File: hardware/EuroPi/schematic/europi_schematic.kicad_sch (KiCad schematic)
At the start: 110 parts, among them J1 Output 1 Jack, J2 Output 2 Jack, J3 Output 3 Jack, J4 Output 4 Jack, J5 Output 5 Jack, J6 Output 6 Jack, J7 Digital Input Jack, J8 Analogue Input Jack, Q1 2N2222, SW1 SW_Push, SW2 SW_Push

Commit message: create kicad project
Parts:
- removed D1, D2, D3, D4: ${SIM.PARAMS}, symbol Simulation_SPICE:DIODE
- removed Reference? (x5): +12V, symbol text:TEXT
- removed Reference? (x2): +5V, symbol text:TEXT
- removed Reference? (x9): +3.3V, symbol text:TEXT
- added C15: 1nF, Capacitor_SMD:C_0603_1608Metric, symbol Device:C
- added D1, D2, D3, D5: D, symbol Device:D
- added J2: Conn_01x04_Pin, symbol Connector:Conn_01x04_Pin
- C1: renamed from C15; footprint (none) -> Capacitor_SMD:C_0603_1608Metric
- C10: renamed from C7; footprint (none) -> Capacitor_SMD:C_0603_1608Metric
- C11: renamed from C9; footprint (none) -> Capacitor_SMD:C_0603_1608Metric
- C12: footprint (none) -> Capacitor_SMD:C_0603_1608Metric
- C13: renamed from C10; footprint (none) -> Capacitor_SMD:C_0603_1608Metric
- C14: renamed from C13; footprint (none) -> Capacitor_SMD:C_0603_1608Metric
- C16: renamed from C11; footprint (none) -> Capacitor_SMD:C_0603_1608Metric
- C17: renamed from C14; footprint (none) -> Capacitor_SMD:C_0603_1608Metric
- C2: renamed from C16; footprint (none) -> Capacitor_SMD:C_0603_1608Metric
- C3: renamed from C2; footprint (none) -> Capacitor_SMD:C_0603_1608Metric
- C4: renamed from C3; footprint (none) -> Capacitor_SMD:C_0603_1608Metric
- C5: renamed from C4; footprint (none) -> Capacitor_SMD:C_0603_1608Metric
- C6: renamed from C5; footprint (none) -> Capacitor_SMD:C_0603_1608Metric
- C7: renamed from C6; footprint (none) -> Capacitor_SMD:C_0603_1608Metric
- C8: renamed from C1; footprint (none) -> Capacitor_SMD:C_0603_1608Metric
- C9: renamed from C8; footprint (none) -> Capacitor_SMD:C_0603_1608Metric
- J1: renamed from J?; footprint (none) -> Connector_PinHeader_2.54mm:PinHeader_2x08_P2.54mm_Vertical
- J10: renamed from J6; footprint (none) -> Connector_Audio:Jack_3.5mm_QingPu_WQP-PJ398SM_Vertical_CircularHoles
- J3: renamed from J1; footprint (none) -> Connector_Audio:Jack_3.5mm_QingPu_WQP-PJ398SM_Vertical_CircularHoles
- J4: footprint (none) -> Connector_Audio:Jack_3.5mm_QingPu_WQP-PJ398SM_Vertical_CircularHoles
- J5: renamed from J8; footprint (none) -> Connector_Audio:Jack_3.5mm_QingPu_WQP-PJ398SM_Vertical_CircularHoles
- J6: renamed from J2; footprint (none) -> Connector_Audio:Jack_3.5mm_QingPu_WQP-PJ398SM_Vertical_CircularHoles
- J7: renamed from J5; footprint (none) -> Connector_Audio:Jack_3.5mm_QingPu_WQP-PJ398SM_Vertical_CircularHoles
- J8: renamed from J7; footprint (none) -> Connector_Audio:Jack_3.5mm_QingPu_WQP-PJ398SM_Vertical_CircularHoles
- J9: renamed from J3; footprint (none) -> Connector_Audio:Jack_3.5mm_QingPu_WQP-PJ398SM_Vertical_CircularHoles
- LED1, LED6: footprint (none) -> LED_THT:LED_D3.0mm
- LED2: renamed from LED4; footprint (none) -> LED_THT:LED_D3.0mm
- LED3: renamed from LED2; footprint (none) -> LED_THT:LED_D3.0mm
- LED4: renamed from LED5; footprint (none) -> LED_THT:LED_D3.0mm
- LED5: renamed from LED3; footprint (none) -> LED_THT:LED_D3.0mm
- R1: renamed from R20; footprint (none) -> Resistor_SMD:R_0603_1608Metric
- R10: renamed from R38; footprint (none) -> Resistor_SMD:R_0603_1608Metric
- R11: renamed from R13; footprint (none) -> Resistor_SMD:R_0603_1608Metric
- R12: renamed from R16; footprint (none) -> Resistor_SMD:R_0603_1608Metric
- R13: renamed from R7; footprint (none) -> Resistor_SMD:R_0603_1608Metric
- R14: renamed from R10; footprint (none) -> Resistor_SMD:R_0603_1608Metric
- R15: renamed from R28; footprint (none) -> Resistor_SMD:R_0603_1608Metric
- R16: renamed from R2; footprint (none) -> Resistor_SMD:R_0603_1608Metric
- R17: renamed from R5; footprint (none) -> Resistor_SMD:R_0603_1608Metric
- R18: renamed from R21; footprint (none) -> Resistor_SMD:R_0603_1608Metric
- R19: renamed from R30; footprint (none) -> Resistor_SMD:R_0603_1608Metric
- R2: renamed from R19; footprint (none) -> Resistor_SMD:R_0603_1608Metric
- R20: renamed from R33; footprint (none) -> Resistor_SMD:R_0603_1608Metric
- R21: renamed from R36; footprint (none) -> Resistor_SMD:R_0603_1608Metric
- R22: renamed from R39; footprint (none) -> Resistor_SMD:R_0603_1608Metric
- R23: renamed from R22; footprint (none) -> Resistor_SMD:R_0603_1608Metric
- R24: renamed from R14; footprint (none) -> Resistor_SMD:R_0603_1608Metric
- R25: renamed from R17; footprint (none) -> Resistor_SMD:R_0603_1608Metric
- R26: renamed from R8; footprint (none) -> Resistor_SMD:R_0603_1608Metric
- R27: renamed from R11; footprint (none) -> Resistor_SMD:R_0603_1608Metric
- R28: renamed from R23; footprint (none) -> Resistor_SMD:R_0603_1608Metric
- R29: renamed from R3; footprint (none) -> Resistor_SMD:R_0603_1608Metric
- R3: renamed from R1; footprint (none) -> Resistor_SMD:R_0603_1608Metric
- R30: renamed from R6; footprint (none) -> Resistor_SMD:R_0603_1608Metric
- R31, R4: footprint (none) -> Resistor_SMD:R_0603_1608Metric
- R32: renamed from R34; footprint (none) -> Resistor_SMD:R_0603_1608Metric
- R33: renamed from R37; footprint (none) -> Resistor_SMD:R_0603_1608Metric
- R34: renamed from R40; footprint (none) -> Resistor_SMD:R_0603_1608Metric
- R35: renamed from R27; footprint (none) -> Resistor_SMD:R_0603_1608Metric
- R36: renamed from R15; footprint (none) -> Resistor_SMD:R_0603_1608Metric
- R37: renamed from R18; footprint (none) -> Resistor_SMD:R_0603_1608Metric
- R38: renamed from R9; footprint (none) -> Resistor_SMD:R_0603_1608Metric
- R39: renamed from R12; footprint (none) -> Resistor_SMD:R_0603_1608Metric
- R40: renamed from R26; footprint (none) -> Resistor_SMD:R_0603_1608Metric
- R5: renamed from R24; footprint (none) -> Resistor_SMD:R_0603_1608Metric
- R6: renamed from R25; footprint (none) -> Resistor_SMD:R_0603_1608Metric
- R7: renamed from R29; footprint (none) -> Resistor_SMD:R_0603_1608Metric
- R8: renamed from R32; footprint (none) -> Resistor_SMD:R_0603_1608Metric
- R9: renamed from R35; footprint (none) -> Resistor_SMD:R_0603_1608Metric
- U2: renamed from U?; footprint (none) -> Module:RaspberryPi_Pico_Common_THT
- VR1, VR2: footprint (none) -> Potentiometer_THT:Potentiometer_Alpha_RD901F-40-00D_Single_Vertical
- gave numbers to parts that had none: 6
- renumbered O1 to O4, O to O5
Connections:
- net GP16 is gone; now on net OUT_3: R29.2
- net GP17 is gone; now on net OUT_4: R4.2
- net GP18 is gone; now on net OUT_5: R17.2
- net GP19 is gone; now on net OUT_6: R30.2
- net GP20 is gone; now on net OUT_2: R16.2
- net GP21 is gone; now on net OUT_1: R3.2
- net GP22 is gone; now on net DIGITAL_IN: Q1.3 (C), R40.2
- net GP26 is gone; now on net ANALOGUE_IN: O4.1, R28.2
- net GP27 is gone; now on net KNOB_1: VR1.2
- net GP28 is gone; now on net KNOB_2: VR2.2
- net GP4 is gone; now on net BUTTON_1: C9.1, R1.1, R5.1
- net GP5 is gone; now on net BUTTON_2: C10.1, R2.1, R6.1
- net -12V: now also D1.2 (A)
- net GND: now also J5.S, D3.2 (A)
- net +12V: now reaches C1.1, C4.1, C6.1
- net +12V: now also O1.4 (V+), O3.4 (V+), U1.1 (IN), D5.1 (K)
- net OLED_SDA: now reaches U2.1 (GP0)
- net DIN_DETECT: now reaches U2.10 (GP7)
- net DIN_DETECT: now also J8.TN
- net OLED_SCL: now reaches U2.2 (GP1)
- net OUT_3: now reaches U2.21 (GP16)
- net OUT_4: now reaches U2.22 (GP17)
- net OUT_5: now reaches U2.24 (GP18)
- net OUT_6: now reaches U2.25 (GP19)
- net OUT_2: now reaches U2.26 (GP20)
- net OUT_1: now reaches U2.27 (GP21)
- net DIGITAL_IN: now reaches U2.29 (GP22)
- net ANALOGUE_IN: now reaches U2.31 (GP26)
- net ANALOGUE_IN: now also C15.2
- net KNOB_1: now reaches U2.32 (GP27)
- net KNOB_2: now reaches U2.34 (GP28)
- net +3.3V: now reaches C8.1, U2.36 (3V3)
- net +3.3V: now also O4.8 (V+), R40.1, R5.2, R6.2, VR1.1, VR2.1
- net at U2.39 (VSYS): now also D2.1 (K)
- net I2C_SDA: now reaches U2.4 (GP2)
- net I2C_SCL: now reaches U2.5 (GP3)
- net BUTTON_1: now reaches U2.6 (GP4)
- net BUTTON_2: now reaches U2.7 (GP5)
- net AIN_DETECT: now reaches U2.9 (GP6)
- net AIN_DETECT: now also J5.TN
- net at Q1.2 (B), R35.2: now also D3.1 (K)
- net +5V: now reaches C3.1, U1.3 (OUT)
- net +5V: now also D2.2 (A)
- net at J1.1 (Pin_1), J1.10 (Pin_10): now also D5.2 (A)
- net at J1.5 (Pin_5), J1.6 (Pin_6): now also D1.1 (K)
- net at O4.2 (-), R23.2, R28.1: now also C15.1
- no-connect marks 3 -> 17
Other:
- note removed: "Power Rail Filtering"
- moved on the sheet: C1, C10, C2, C4, C5, C6, C7, C8, C9, J5, J8, Q1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

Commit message: rough layout
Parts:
- J1: footprint Connector_PinHeader_2.54mm:PinHeader_2x08_P2.54mm_Vertical -> allen-synthesis:power-header-10-pin
- J10, J3, J4, J5, J6, J7, J8, J9: footprint Connector_Audio:Jack_3.5mm_QingPu_WQP-PJ398SM_Vertical_CircularHoles -> allen-synthesis:jack-thonkiconn-mono
- LED1, LED2, LED3, LED4, LED5, LED6: footprint LED_THT:LED_D3.0mm -> allen-synthesis:led-3mm
- SW1, SW2: footprint (none) -> allen-synthesis:switch-momentary-c&k
- VR1, VR2: footprint Potentiometer_THT:Potentiometer_Alpha_RD901F-40-00D_Single_Vertical -> allen-synthesis:potentiometer-9mm
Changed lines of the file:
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@@
 			)
 		)
-		(property "Footprint" "Connector_Audio:Jack_3.5mm_QingPu_WQP-PJ398SM_Vertical_CircularHoles"
+		(property "Footprint" "allen-synthesis:jack-thonkiconn-mono"
 			(at 375.92 93.98 0)
 			(effects
@@
 			)
 		)
-		(property "Footprint" "LED_THT:LED_D3.0mm"
+		(property "Footprint" "allen-synthesis:led-3mm"
 			(at 167.64 58.42 0)
 			(effects
@@
 			)
 		)
-		(property "Footprint" "LED_THT:LED_D3.0mm"
+		(property "Footprint" "allen-synthesis:led-3mm"
 			(at 261.62 58.42 0)
 			(effects
@@
 			)
 		)
-		(property "Footprint" "LED_THT:LED_D3.0mm"
+		(property "Footprint" "allen-synthesis:led-3mm"
 			(at 356.87 58.42 0)
 			(effects
@@
 			)
 		)
-		(property "Footprint" "LED_THT:LED_D3.0mm"
+		(property "Footprint" "allen-synthesis:led-3mm"
 			(at 167.64 114.3 0)
 			(effects
@@
 			)
 		)
-		(property "Footprint" "LED_THT:LED_D3.0mm"
+		(property "Footprint" "allen-synthesis:led-3mm"
 			(at 261.62 114.3 0)
 			(effects
@@
 			)
 		)
-		(property "Footprint" "LED_THT:LED_D3.0mm"
+		(property "Footprint" "allen-synthesis:led-3mm"
 			(at 356.87 114.3 0)
 			(effects
@@
 			)
 		)
-		(property "Footprint" "Connector_Audio:Jack_3.5mm_QingPu_WQP-PJ398SM_Vertical_CircularHoles"
+		(property "Footprint" "allen-synthesis:jack-thonkiconn-mono"
 			(at 334.01 175.26 0)
 			(effects
@@
 			)
 		)
-		(property "Footprint" "Connector_Audio:Jack_3.5mm_QingPu_WQP-PJ398SM_Vertical_CircularHoles"
+		(property "Footprint" "allen-synthesis:jack-thonkiconn-mono"
 			(at 375.92 38.1 0)
 			(effects
@@
 			)
 		)
-		(property "Footprint" "Connector_Audio:Jack_3.5mm_QingPu_WQP-PJ398SM_Vertical_CircularHoles"
+		(property "Footprint" "allen-synthesis:jack-thonkiconn-mono"
 			(at 280.67 38.1 0)
 			(effects
@@
 			)
 		)
-		(property "Footprint" "Connector_Audio:Jack_3.5mm_QingPu_WQP-PJ398SM_Vertical_CircularHoles"
+		(property "Footprint" "allen-synthesis:jack-thonkiconn-mono"
 			(at 186.69 38.1 0)
 			(effects
@@
 			)
 		)
-		(property "Footprint" "Connector_Audio:Jack_3.5mm_QingPu_WQP-PJ398SM_Vertical_CircularHoles"
+		(property "Footprint" "allen-synthesis:jack-thonkiconn-mono"
 			(at 186.69 93.98 0)
 			(effects
@@
 			)
 		)
-		(property "Footprint" "Connector_Audio:Jack_3.5mm_QingPu_WQP-PJ398SM_Vertical_CircularHoles"
+		(property "Footprint" "allen-synthesis:jack-thonkiconn-mono"
 			(at 280.67 93.98 0)
 			(effects
@@
 			)
 		)
-		(property "Footprint" "Connector_PinHeader_2.54mm:PinHeader_2x08_P2.54mm_Vertical"
+		(property "Footprint" "allen-synthesis:power-header-10-pin"
 			(at 35.56 41.91 0)
 			(effects
@@
 			)
 		)
-		(property "Footprint" "Connector_Audio:Jack_3.5mm_QingPu_WQP-PJ398SM_Vertical_CircularHoles"
+		(property "Footprint" "allen-synthesis:jack-thonkiconn-mono"
 			(at 199.39 173.99 0)
 			(effects
@@
 			)
 		)
-		(property "Footprint" ""
+		(property "Footprint" "allen-synthesis:switch-momentary-c&k"
 			(at 110.49 163.83 0)
 			(effects
@@
 			)
 		)
-		(property "Footprint" ""
+		(property "Footprint" "allen-synthesis:switch-momentary-c&k"
 			(at 110.49 186.69 0)
 			(effects
@@
 			)
 		)
-		(property "Footprint" "Potentiometer_THT:Potentiometer_Alpha_RD901F-40-00D_Single_Vertical"
+		(property "Footprint" "allen-synthesis:potentiometer-9mm"
 			(at 336.55 223.52 0)
 			(effects
@@
 			)
 		)
-		(property "Footprint" "Potentiometer_THT:Potentiometer_Alpha_RD901F-40-00D_Single_Vertical"
+		(property "Footprint" "allen-synthesis:potentiometer-9mm"
 			(at 365.76 223.52 0)
 			(effects

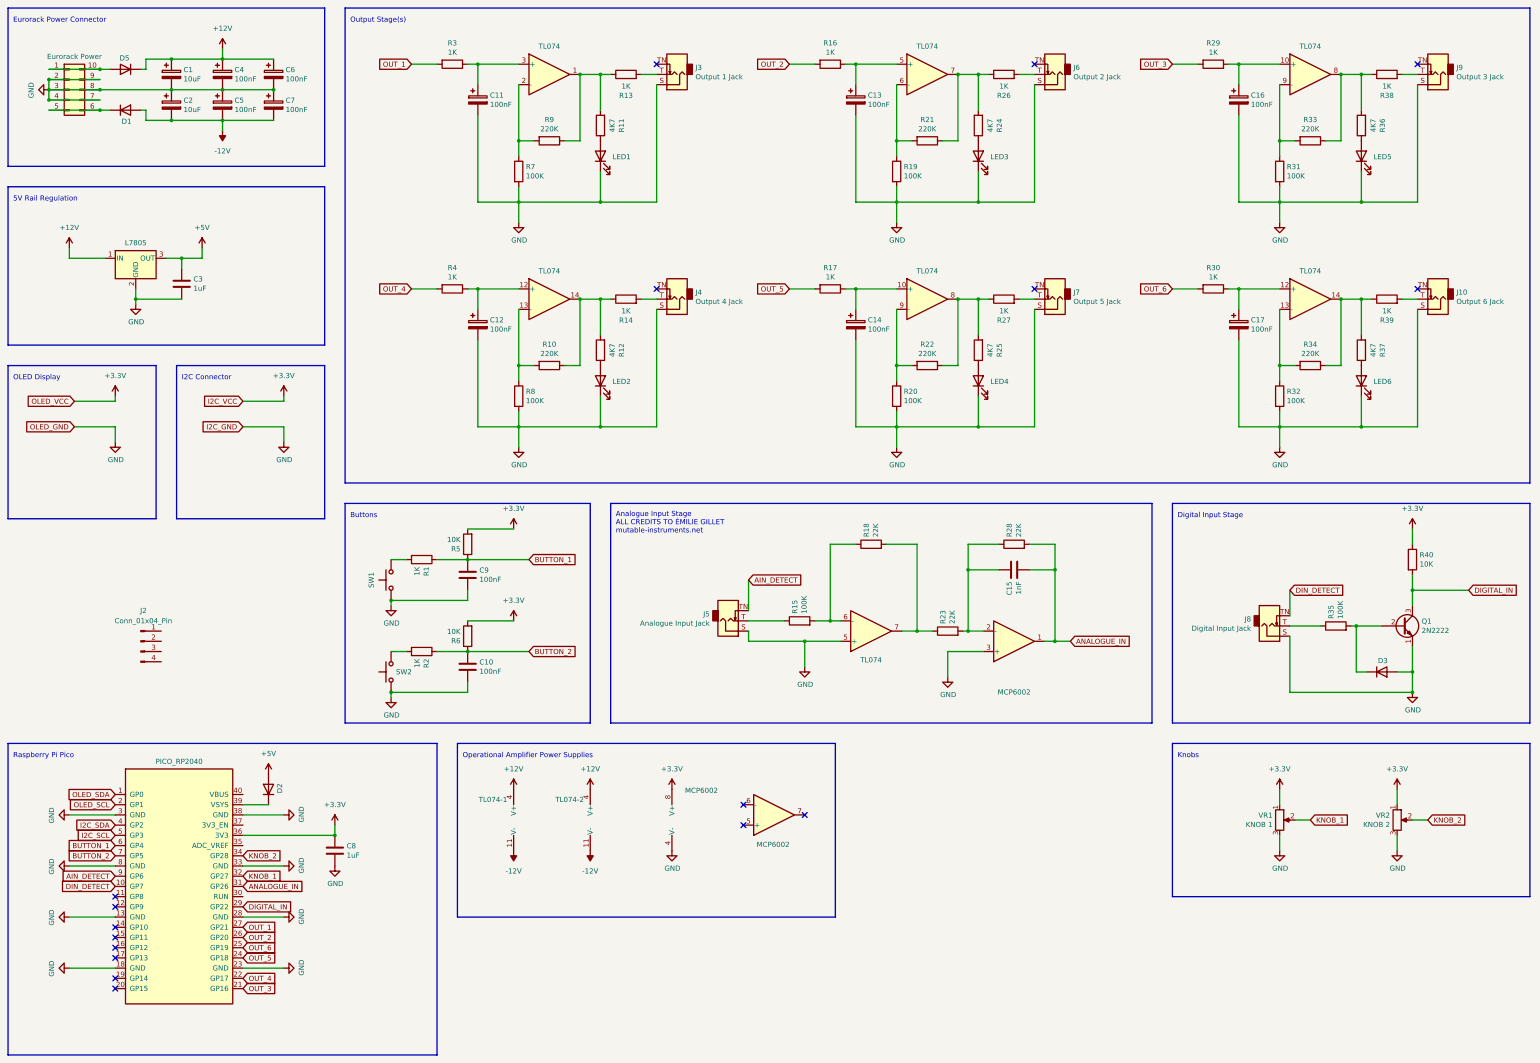
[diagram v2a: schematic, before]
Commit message: passes drc
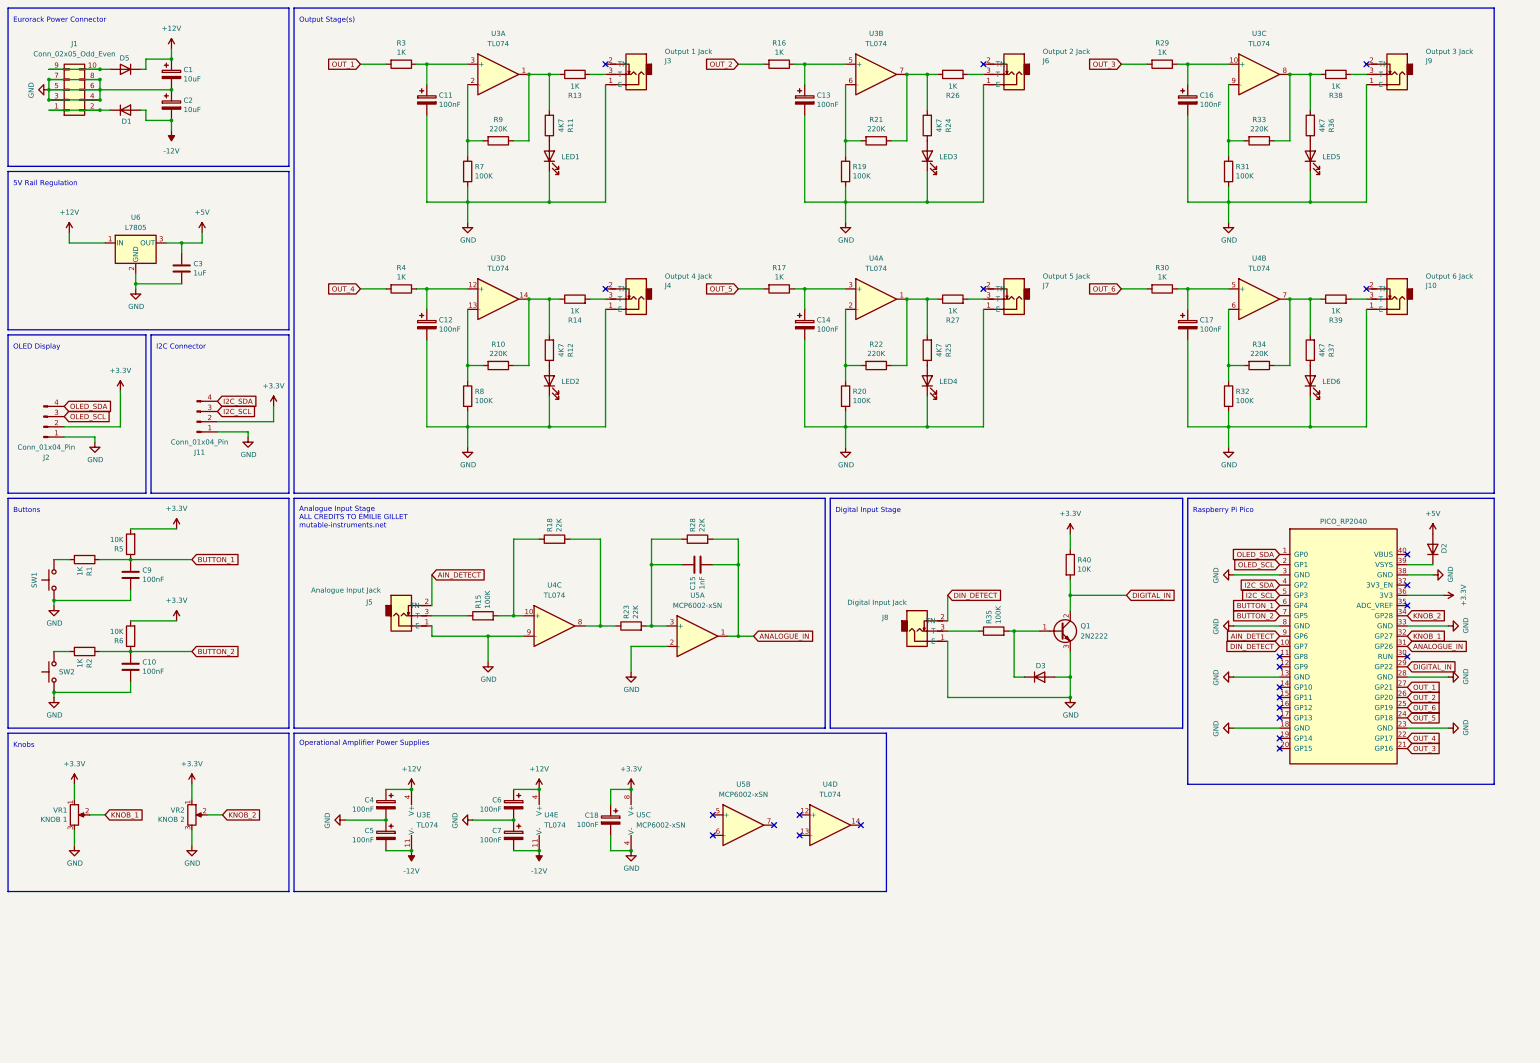
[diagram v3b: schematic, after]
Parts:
- removed C8: 1uF, Capacitor_SMD:C_0603_1608Metric, symbol Device:C
- removed J1: Eurorack Power, allen-synthesis:power-header-10-pin, symbol Connector_Generic:Conn_02x05_Counter_Clockwise
- removed O1: TL074-1, symbol Amplifier_Operational:TL074
- removed O2, O5: TL074, symbol Amplifier_Operational:TL074
- removed O3: TL074-2, symbol Amplifier_Operational:TL074
- removed O4: MCP6002, symbol Amplifier_Operational:MCP6002-xMS
- removed U1: L7805, symbol Regulator_Linear:L7805
- added C18: 100nF, Capacitor_SMD:C_0603_1608Metric, symbol Device:CP
- added J1: Conn_02x05_Odd_Even, allen-synthesis:power-header-10-pin-unlabelled, symbol Connector_Generic:Conn_02x05_Odd_Even
- added J11: Conn_01x04_Pin, Connector_PinHeader_2.54mm:PinHeader_1x04_P2.54mm_Vertical, symbol Connector:Conn_01x04_Pin
- added U3, U4: TL074, Package_SO:SOIC-14_3.9x8.7mm_P1.27mm, symbol Amplifier_Operational:TL074
- added U5: MCP6002-xSN, Package_SO:SOIC-8_3.9x4.9mm_P1.27mm, symbol Amplifier_Operational:MCP6002-xSN
- added U6: L7805, Package_TO_SOT_SMD:TO-252-2, symbol Regulator_Linear:L7805
- C1, C2: footprint Capacitor_SMD:C_0603_1608Metric -> Capacitor_SMD:C_0805_2012Metric
- D1, D2, D5: footprint (none) -> Diode_SMD:D_SMA; LCSC Part (none) -> C5356810
- D3: footprint (none) -> Diode_SMD:D_SMA
- J10, J3, J4, J5, J6, J7, J8, J9: symbol Connector:AudioJack2_SwitchT -> allen-synthesis:jack-thonkiconn-mono
- J2: footprint (none) -> Connector_PinHeader_2.54mm:PinHeader_1x04_P2.54mm_Vertical
- Q1: footprint Package_TO_SOT_THT:TO-39-3 -> Package_TO_SOT_SMD:SOT-89-3; LCSC Part (none) -> C21714170
- U2: footprint Module:RaspberryPi_Pico_Common_THT -> allen-synthesis:raspberry-pi-pico
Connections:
- net +12V: now also U3.4 (V+), U4.4 (V+), U6.1 (IN)
- net +3.3V: now also J2.2 (Pin_2), C18.1, J11.2 (Pin_2), U5.8 (V+)
- net +5V: now also U6.3 (OUT)
- net -12V: now also U3.11 (V-), U4.11 (V-)
- net AIN_DETECT: now also J5.2 (TN); no longer J5.TN
- net ANALOGUE_IN: now also U5.1
- net DIGITAL_IN: now also Q1.2 (C); no longer Q1.3 (C)
- net DIN_DETECT: now also J8.2 (TN); no longer J8.TN
- net GND: now also J10.1 (E), J2.1 (Pin_1), J3.1 (E), J4.1 (E), J5.1 (E), J6.1 (E), J7.1 (E), J8.1 (E), J9.1 (E), Q1.3 (E), C18.2, J1.3 (Pin_3), J1.4 (Pin_4), J1.5 (Pin_5), J1.6 (Pin_6), J1.7 (Pin_7), J1.8 (Pin_8), J11.1 (Pin_1), U4.9 (-), U5.2 (-), U5.4 (V-), U6.2 (GND); no longer J10.S, J3.S, J4.S, J5.S, J6.S, J7.S, J8.S, J9.S, Q1.1 (E)
- net I2C_SCL: now also J11.3 (Pin_3)
- net I2C_SDA: now also J11.4 (Pin_4)
- net OLED_SCL: now also J2.3 (Pin_3)
- net OLED_SDA: now also J2.4 (Pin_4)
- net at C16.1, R29.1: now also U3.10 (+)
- net at R33.1, R36.2, R38.1: now also U3.8
- net at R31.1, R33.2: now also U3.9 (-)
- net at R11.2, R13.1, R9.1: now also U3.1
- net at R7.1, R9.2: now also U3.2 (-)
- net at C11.1, R3.1: now also U3.3 (+)
- net at C13.1, R16.1: now also U3.5 (+)
- net at R19.1, R21.2: now also U3.6 (-)
- net at R21.1, R24.2, R26.1: now also U3.7
- net at C17.1, R30.1: now also U4.5 (+)
- net at R32.1, R34.2: now also U4.6 (-)
- net at R34.1, R37.2, R39.1: now also U4.7
- net at R39.2: now also J10.3 (T); no longer J10.T
- net at C12.1, R4.1: now also U3.12 (+)
- net at R10.2, R8.1: now also U3.13 (-)
- net at R10.1, R12.2, R14.1: now also U3.14
- net at C14.1, R17.1: now also U4.3 (+)
- net at R22.1, R25.2, R27.1: now also U4.1
- net at R20.1, R22.2: now also U4.2 (-)
- net at R35.1: now also J8.3 (T); no longer J8.T
- net at D3.1 (K), R35.2: now also Q1.1 (B); no longer Q1.2 (B)
- net at R38.2: now also J9.3 (T); no longer J9.T
- net at R26.2: now also J6.3 (T); no longer J6.T
- net at R13.2: now also J3.3 (T); no longer J3.T
- net at R14.2: now also J4.3 (T); no longer J4.T
- net at R27.2: now also J7.3 (T); no longer J7.T
- net at D5.2 (A): now also J1.10 (Pin_10), J1.9 (Pin_9)
- net at D1.1 (K): now also J1.1 (Pin_1), J1.2 (Pin_2)
- net at R15.1: now also J5.3 (T); no longer J5.T
- net at R15.2, R18.1: now also U4.10 (+)
- net at R18.2, R23.1: now also U4.8
- net at C15.1, R23.2, R28.1: now also U5.3 (+)
- no-connect marks 17 -> 24
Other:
- moved on the sheet: C10, C11, C12, C13, C14, C15, C16, C17, C3, C4, C5, C6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

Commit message: ordered rev 1
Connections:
- net +3.3V: now also U2.14 (GP10)
- no-connect marks 24 -> 23
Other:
- note added: "0 1 0 0 0 0 0 0"
- note added: "Bit 1 (LSB) Bit 2 Bit 3 Bit 4"
- note added: "EuroPi"
- note added: "EuroPi SMD"
- moved on the sheet: D2
